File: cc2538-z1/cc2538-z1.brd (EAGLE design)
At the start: 56.8 x 34.5 mm, 90 parts, among them J2 2-PIN-MOLEX, Q2 DMG6602SVT, U1 CC2538, U2 CC1120_RHM_32, U3 TPD2E001IDRLRQ1, U4 CP2103, U5 BSS138PS, U6 BSS138PS, U7 BSS138PS, X1 FA-128, X2 32MHz, X3 32.768K

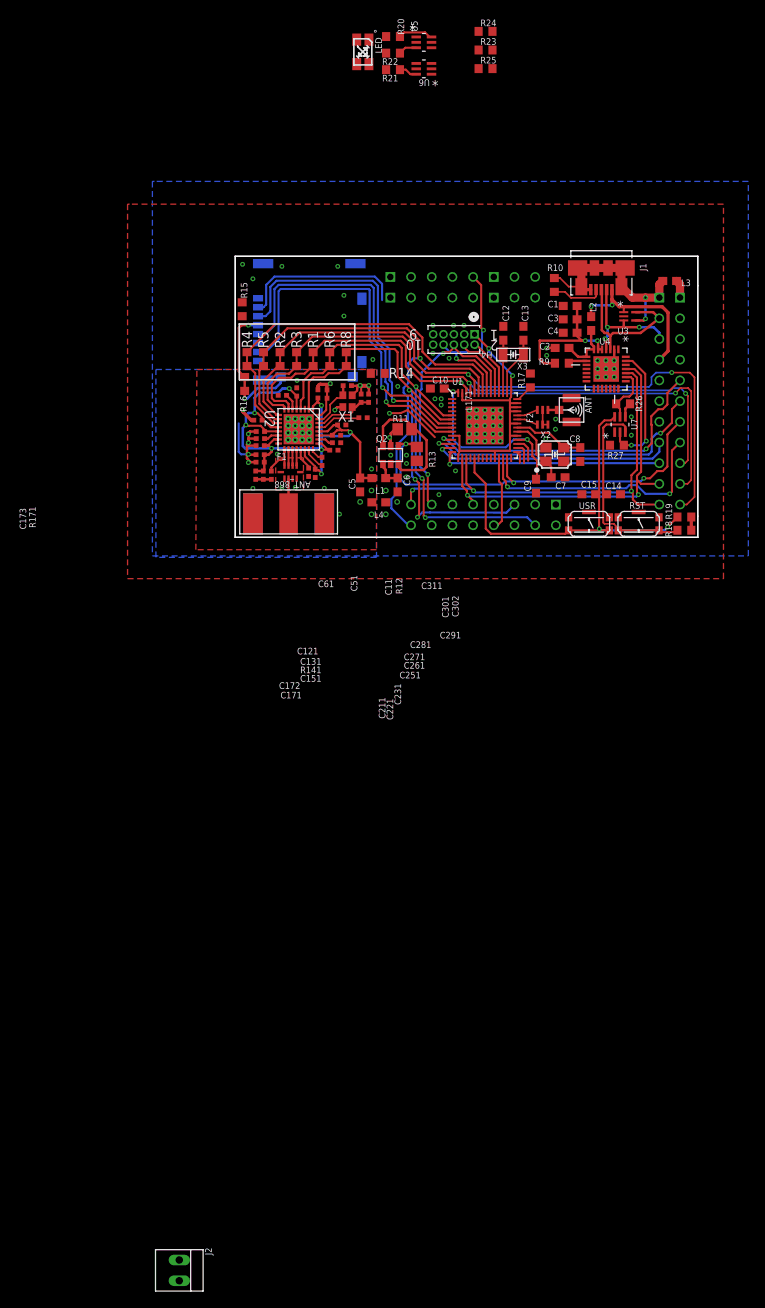
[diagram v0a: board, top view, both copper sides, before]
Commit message: Moved to a 4-layer board.
Updated DRU to meet Euro Circuits Class 6C pool service.

22 airwires left

TODO: Check SD card SEL implementation.
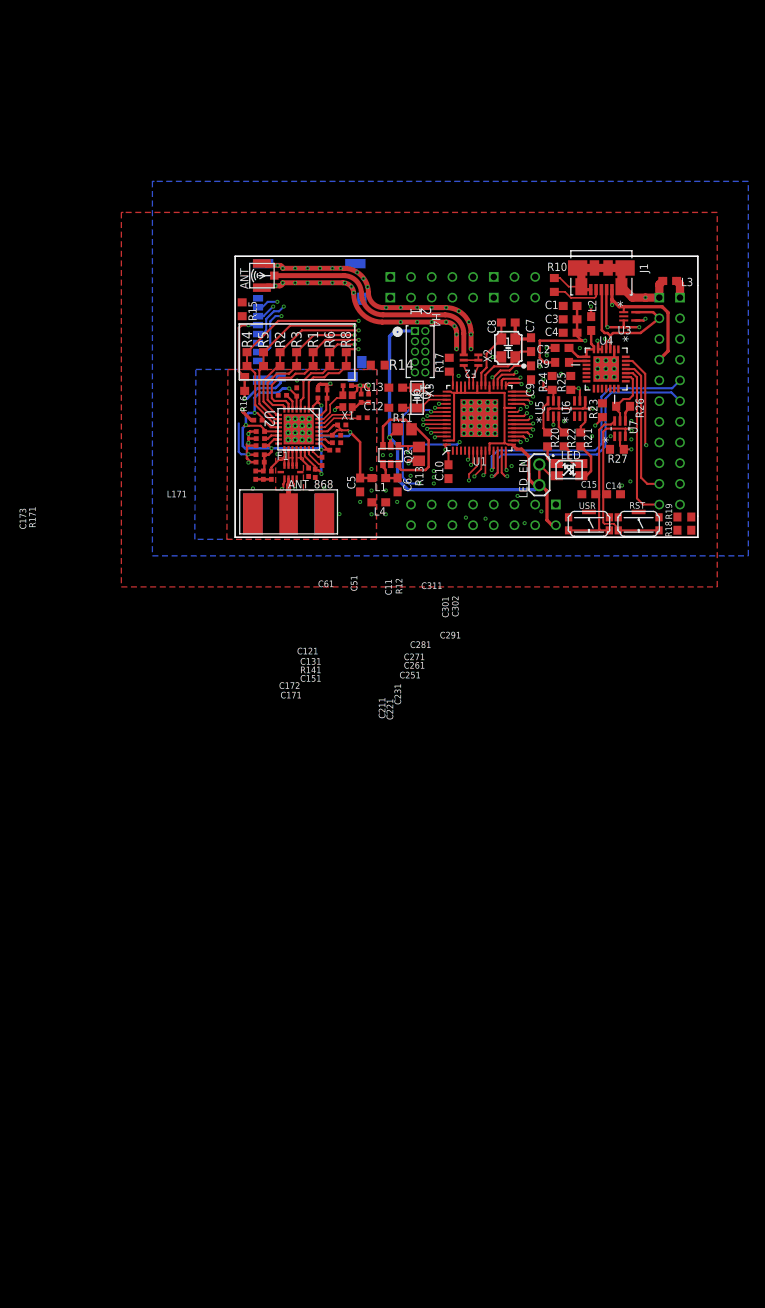
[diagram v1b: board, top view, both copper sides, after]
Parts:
- removed J2: 2-PIN-MOLEX, farnell-parts:2-MOLEX
- moved LED 57.2 mm to (41.0, 8.31), turned to 270 degrees
- moved R20 53.0 mm to (38.4, 12.0), turned to 270 degrees
- moved R22 51.9 mm to (40.4, 12.0), turned to 270 degrees
- moved R21 50.9 mm to (42.4, 12.0), turned to 270 degrees
- moved U5 47.7 mm to (39.1, 15.8), turned to 90 degrees
- moved R23 46.5 mm to (45.1, 15.6), turned to 90 degrees
- moved U6 45.9 mm to (42.3, 15.8), turned to 90 degrees
- moved R24 43.9 mm to (38.9, 18.9), turned to 90 degrees
- moved ANT 41.4 mm to (3.28, 32.1), turned to 90 degrees
- moved R25 40.0 mm to (41.2, 18.9), turned to 90 degrees
- moved C8 18.5 mm to (33.5, 26.4), turned to 180 degrees
- moved C13 17.0 mm to (19.7, 18.4), turned to 0 degrees
- moved C7 16.6 mm to (36.3, 23.6), turned to 270 degrees
- moved C12 16.1 mm to (19.7, 15.9), turned to 0 degrees
- moved X2 14.3 mm to (33.5, 23.2), turned to 90 degrees
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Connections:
- net +3V3: no longer J2.1, J2.2
- net GND: now also U6.4; no longer U6.1
- net LEDS_BLUE: now also U6.5; no longer U6.2
- net N$32: now also U6.3; no longer U6.6
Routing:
- net GND: track 27.3 -> 136.2 mm, vias 67 -> 86
- net +3V3: track 44.1 -> 91.1 mm
- net CC2538_NRESET: track 25.9 -> 58.4 mm, vias 0 -> 4
- net USER_BUTTON: track 51.1 -> 23.1 mm, vias 2 -> 1
- net 2.4G: track 1.38 -> 28.8 mm
- net SD_SPI_CSN: track 20.6 -> 44.3 mm, vias 0 -> 2
- net LEDS_RED: track 3.10 -> 23.0 mm, vias 0 -> 5
- net RADIO_SPI_CSN: track 47.2 -> 65.1 mm, vias 0 -> 2
- net LEDS_BLUE: track 1.54 -> 12.2 mm, vias 0 -> 2
- net UART0_TX: track 54.1 -> 63.9 mm, vias 3 -> 2
- net RADIO_RESET_N: track 58.4 -> 49.1 mm
- net LEDS_GREEN: track 2.52 -> 9.61 mm, vias 0 -> 2
- net RS485_TXEN: track 9.07 -> 2.00 mm, vias 0 -> 1
- net SD_SPI_MISO: track 43.5 -> 50.2 mm, vias 1 -> 3
- net PWR_SENSE_EN: track 31.4 -> 24.8 mm, vias 2 -> 1
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- added copper zone on layer 2, net GND
- added copper zone on layer 3, net GND
- added copper zone on layer 2, net RGND
- added copper zone on layer 3, net RGND
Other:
- board text added: "LED_EN"

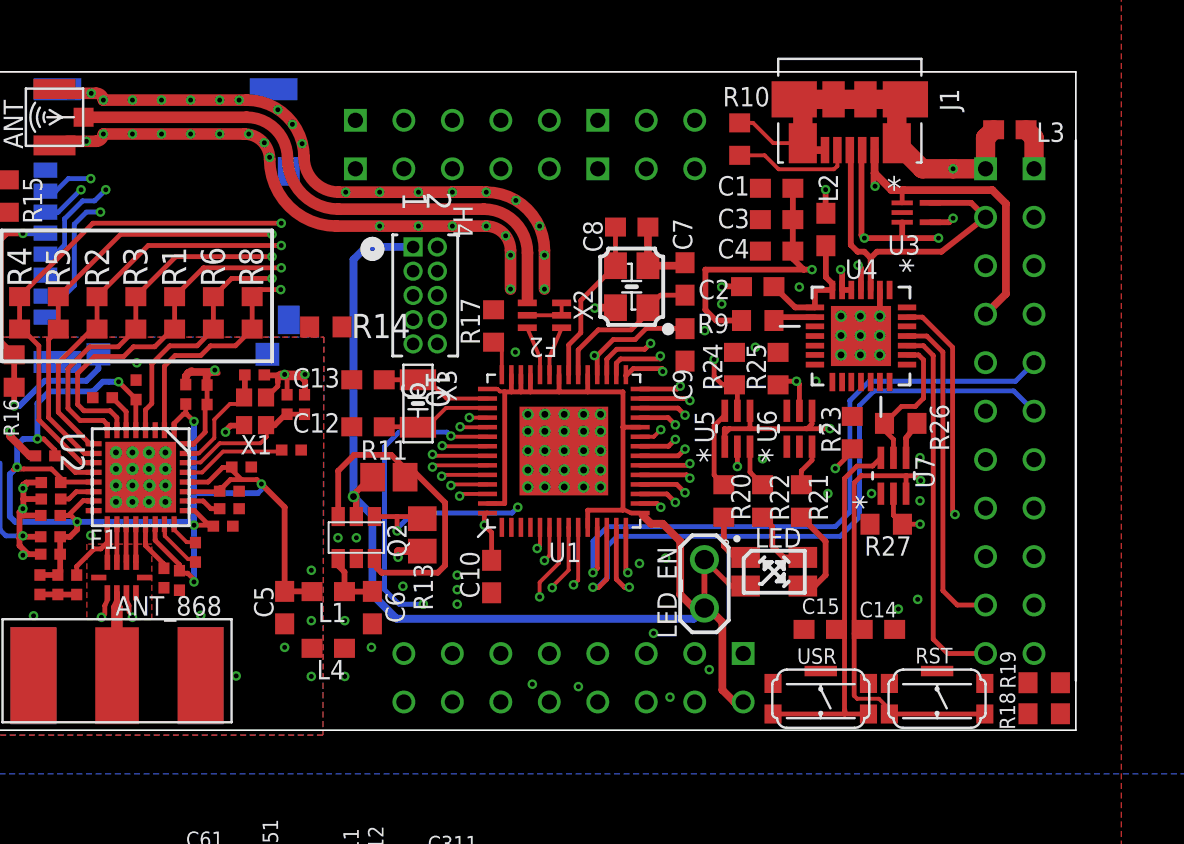
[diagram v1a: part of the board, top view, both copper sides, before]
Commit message: A lot of work on 4-layer CC2538/1120 design.
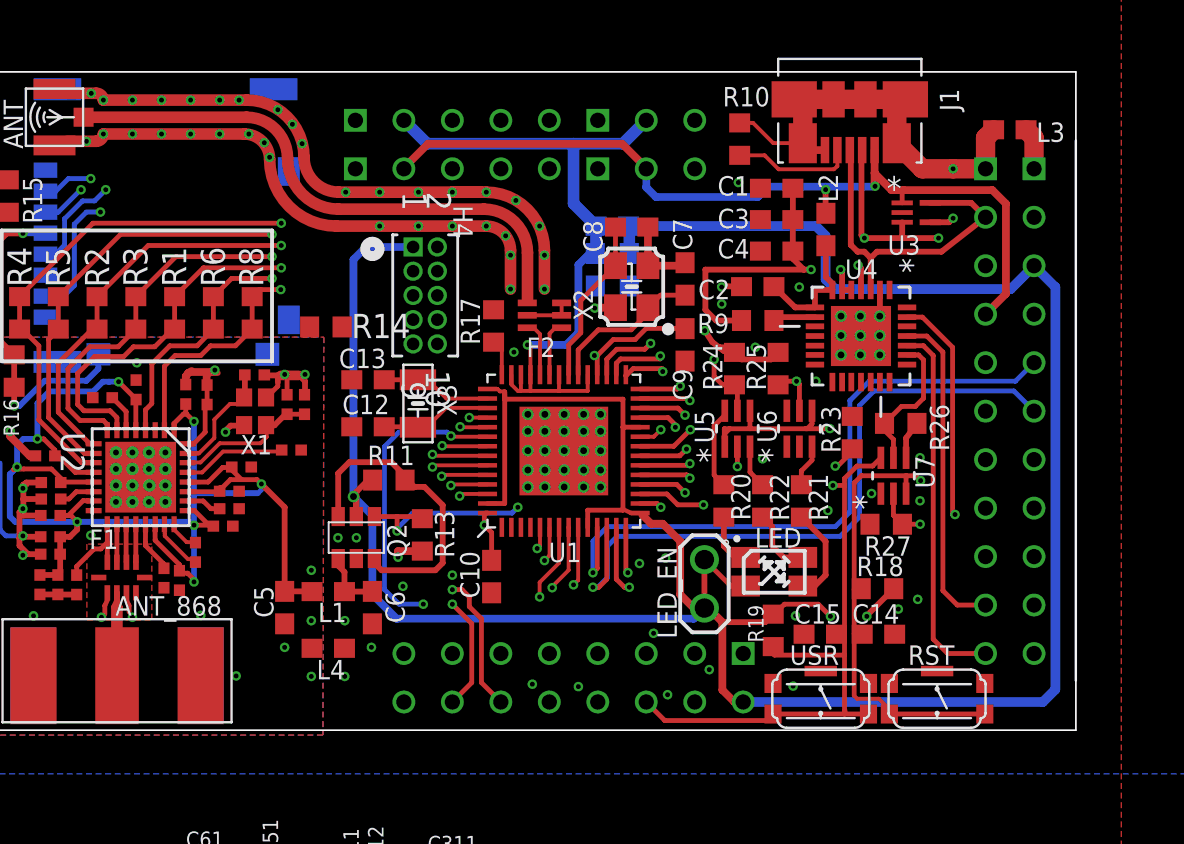
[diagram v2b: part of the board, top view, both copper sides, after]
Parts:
- added C16, C17: 100nf, CC11x:C0603
- added L5: BEAD, CC11x:C0603
- R11, R13: device resistor:R0805 -> rcl:R0603
- moved R19 14.5 mm to (40.9, 5.23), turned to 90 degrees
- moved R18 10.9 mm to (46.4, 7.42)
- moved C14 0.25 mm to (46.5, 5.03)
- moved C15 0.25 mm to (43.4, 5.03)
- moved R11 0.15 mm to (20.8, 13.1)
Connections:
- removed net N$38: H1.A14, H1.A4
- removed net N$47: H1.A1, H1.A11, H1.A12, H1.A2
- removed net N$63: H1.B20
- new net +3V3_ANALOGUE: C17.1, H1.A14, H1.A4, L5.1, U1.33, U1.36, U1.39, U1.40, U1.41
- new net N$35: H1.A15
- new net N$36: H1.A5
- new net N$37: H1.A7
- new net N$39: H1.A8
- new net N$40: H1.C41
- net +3V3: now also C16.1, L5.2; no longer U1.33, U1.36, U1.39, U1.40, U1.41
- net +3V3_SERIAL: now also H1.B20
- net GND: now also C16.2, C17.2, H1.A1, H1.A11, H1.A12, H1.A2
- net SD_SPI_CLK: now also H1.C45
- net SD_SPI_MISO: now also H1.C52
- net SD_SPI_MOSI: now also H1.C50
- net USER_BUTTON: now also H1.C44
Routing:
- net +3V3: track 91.1 -> 162.0 mm, vias 3 -> 5
- net ADC_SENSORS_ADC3: track 2.53 -> 42.3 mm, vias 1 -> 2
- net +3V3_ANALOGUE: track 0.00 -> 37.3 mm, vias 0 -> 1
- net ADC_SENSORS_ADC2: track 2.64 -> 35.4 mm
- net +5V_USB: track 20.5 -> 45.1 mm
- net ADC_SENSORS_ADC1: track 2.50 -> 22.7 mm
- net RS485_TXEN: track 2.00 -> 22.0 mm
- net USER_BUTTON: track 23.1 -> 42.8 mm, vias 1 -> 2
- net +3V3_SERIAL: track 17.8 -> 29.8 mm
- net SD_SPI_MOSI: track 47.3 -> 54.5 mm
- net SD_SPI_MISO: track 50.2 -> 56.2 mm
- net GND: track 136.2 -> 141.4 mm, vias 86 -> 88
- net SD_SPI_CLK: track 49.3 -> 53.7 mm
- net N$34: track 17.4 -> 16.1 mm
- net SD_SEL: track 19.7 -> 20.7 mm

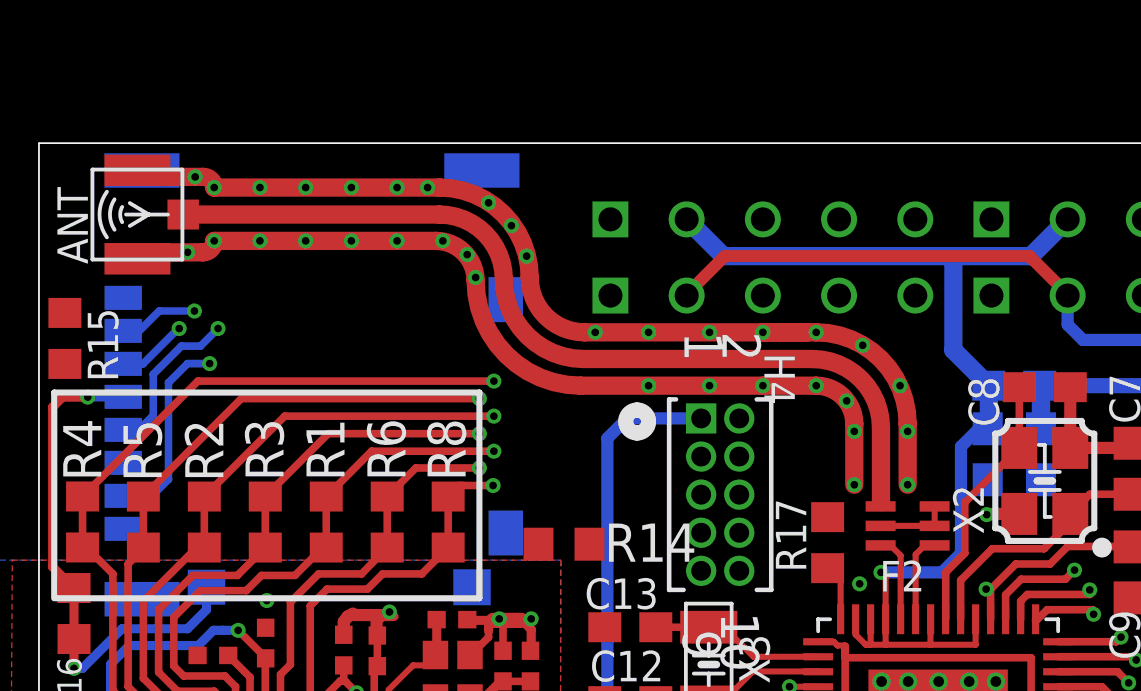
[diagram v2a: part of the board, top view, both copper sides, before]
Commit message: All traces apart from SDSEL routed. Need to tweak RF layout
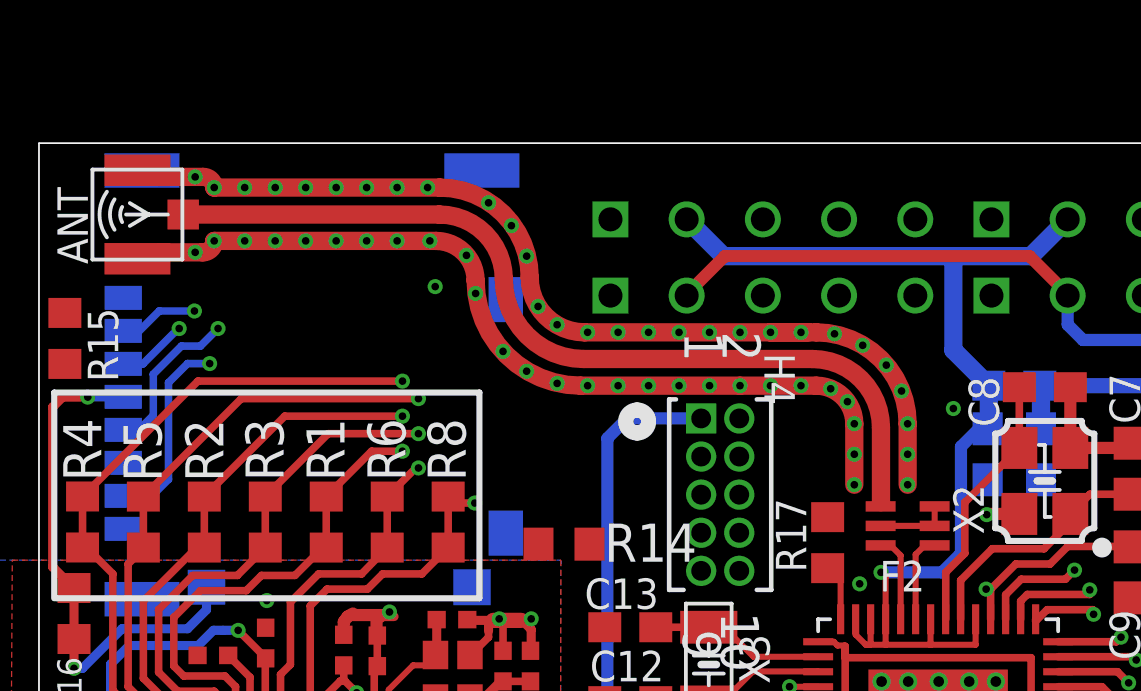
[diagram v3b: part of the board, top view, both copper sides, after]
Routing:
- net SD_SEL: track 20.7 -> 59.4 mm, vias 3 -> 5
- net JTAG_TDI/DIO2: track 25.4 -> 27.7 mm
- net RADIO_RESET_N: track 49.1 -> 48.4 mm
- net RADIO_SPI_MISO: track 82.0 -> 81.4 mm
- net RADIO_SPI_CSN: track 65.1 -> 64.5 mm
- net RADIO_SPI_CLK: track 74.0 -> 73.4 mm
- net RADIO_SPI_MOSI: track 73.2 -> 72.6 mm
- net RADIO_GPIO0: track 65.8 -> 65.2 mm
- net RADIO_GPIO2: track 54.9 -> 54.4 mm
- net GND: track 141.4 -> 141.1 mm, vias 88 -> 109

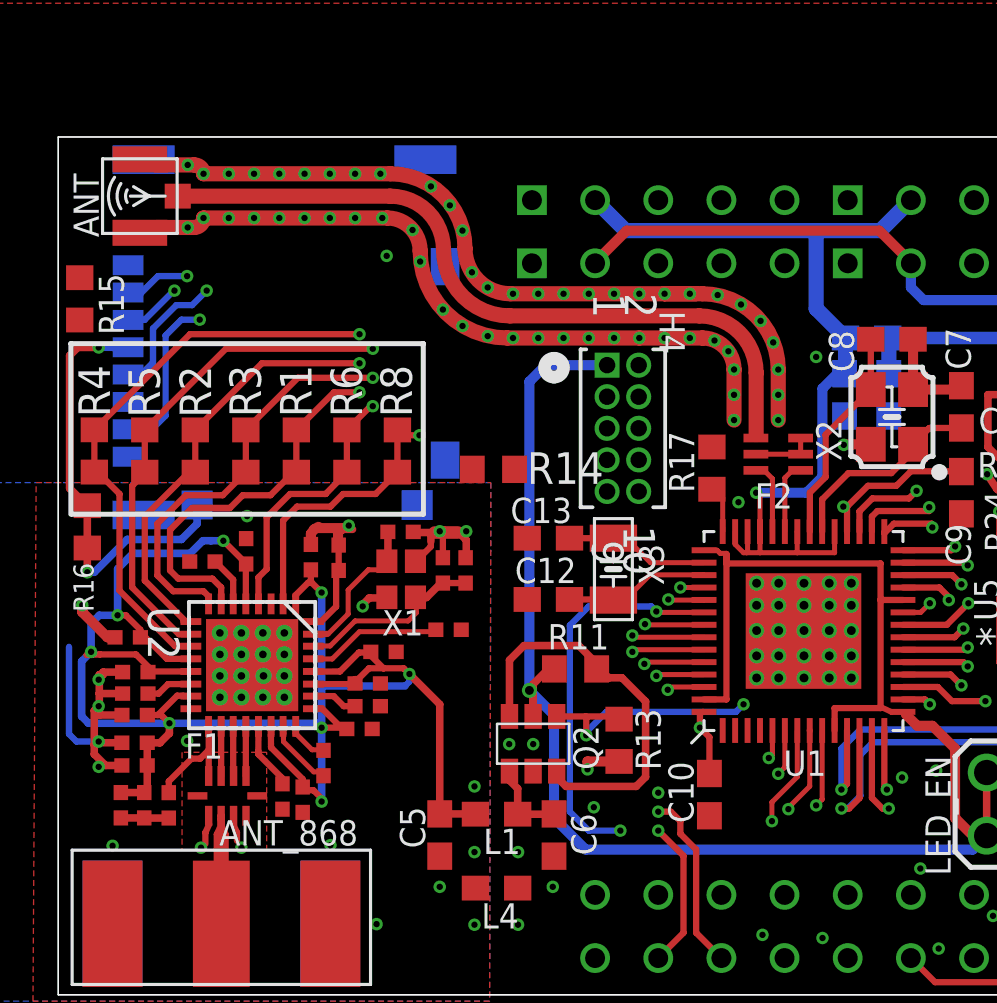
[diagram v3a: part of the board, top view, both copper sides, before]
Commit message: Sorted out the RF traces a bit.
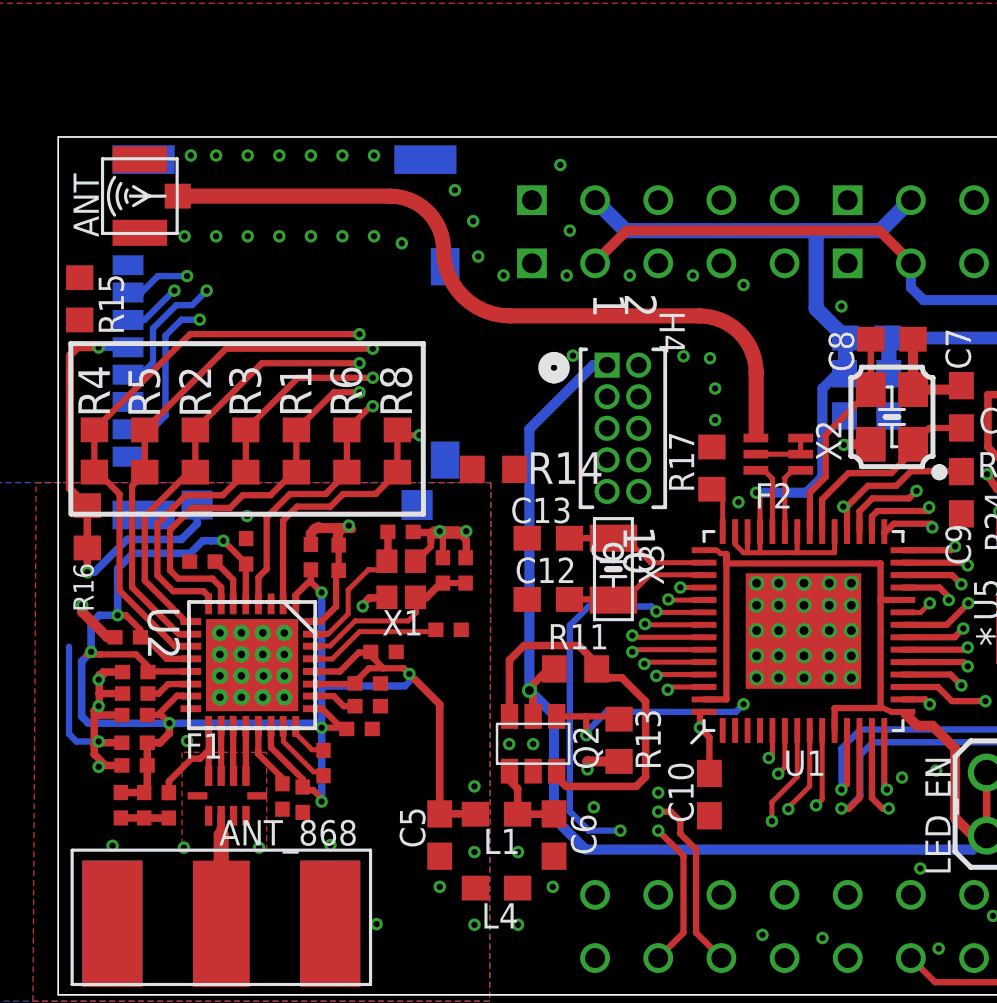
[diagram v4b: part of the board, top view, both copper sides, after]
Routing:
- net GND: track 141.1 -> 81.5 mm, vias 109 -> 82
- net RGND: track 33.5 -> 31.9 mm
- net +3V3: track 162.0 -> 160.9 mm
- net SD_SEL: track 59.4 -> 58.4 mm
